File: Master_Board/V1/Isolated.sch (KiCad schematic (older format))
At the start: 0 parts

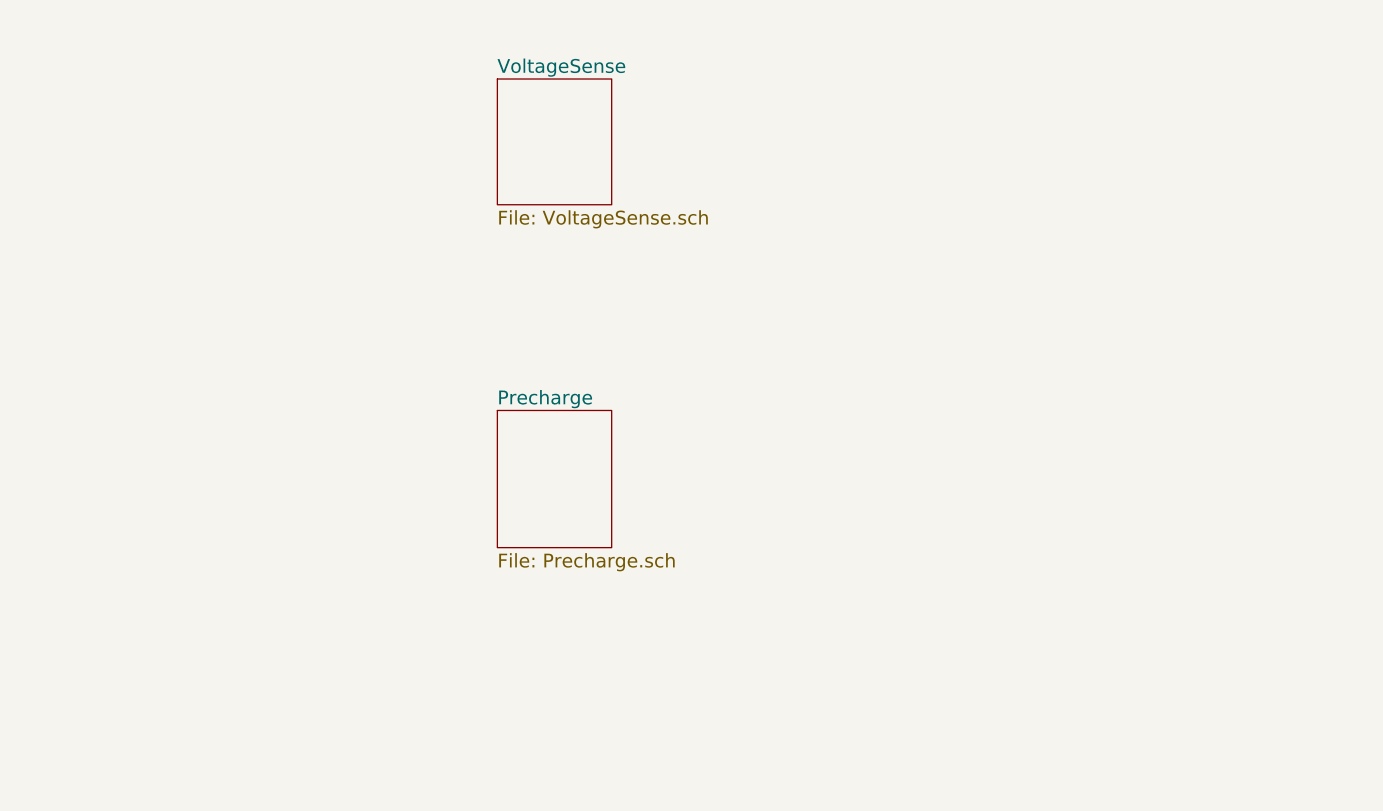
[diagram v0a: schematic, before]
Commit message: Add Master_Board modules
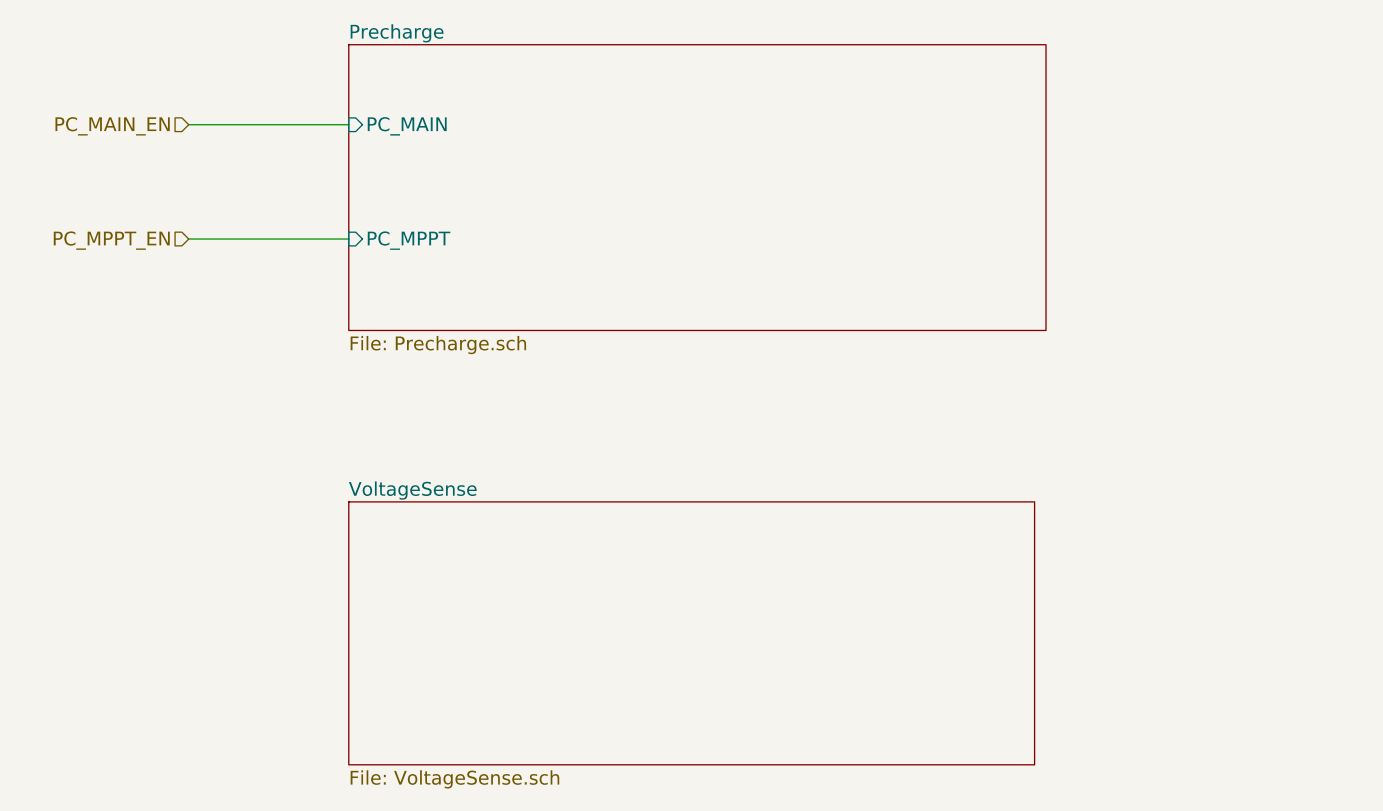
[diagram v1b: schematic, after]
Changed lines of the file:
@@
 $EndDescr
 $Sheet
-S 4700 2600 500  550
+S 4050 2450 3050 1250
+U 5941231F
+F0 "Precharge" 60
+F1 "Precharge.sch" 60
+F2 "PC_MAIN" I L 4050 2800 60
+F3 "PC_MPPT" I L 4050 3300 60
+$EndSheet
+Text HLabel 3350 2800 0    60   Input ~ 0
+PC_MAIN_EN
+$Sheet
+S 4050 4450 3000 1150
 U 5941231C
 F0 "VoltageSense" 60
 F1 "VoltageSense.sch" 60
 $EndSheet
-$Sheet
-S 4700 4050 500  600
-U 5941231F
-F0 "Precharge" 60
-F1 "Precharge.sch" 60
-$EndSheet
+Text HLabel 3350 3300 0    60   Input ~ 0
+PC_MPPT_EN
+Wire Wire Line
+	3350 2800 4050 2800
+Wire Wire Line
+	3350 3300 4050 3300
 $EndSCHEMATC

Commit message: git modify Master_board
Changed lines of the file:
@@
 F0 "VoltageSense" 60
 F1 "VoltageSense.sch" 60
+F2 "BP_VSense" I L 4050 4700 60
+F3 "VSense_EN" I L 4050 5000 60
+F4 "MPPT_VSense" I L 4050 5300 60
 $EndSheet
 Text HLabel 3350 3300 0    60   Input ~ 0
@@
 Wire Wire Line
 	3350 3300 4050 3300
+Wire Wire Line
+	4050 4700 3350 4700
+Wire Wire Line
+	4050 5000 3350 5000
+Wire Wire Line
+	4050 5300 3350 5300
+Text HLabel 3350 4700 0    60   Input ~ 0
+BP_VSense
+Text HLabel 3350 5000 0    60   Input ~ 0
+VSense_EN
+Text HLabel 3350 5300 0    60   Input ~ 0
+MPPT_VSense
 $EndSCHEMATC

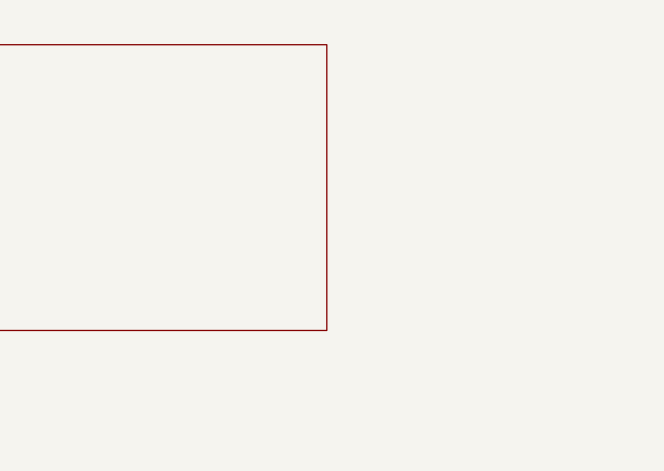
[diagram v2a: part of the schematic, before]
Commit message: Add page LedDriver
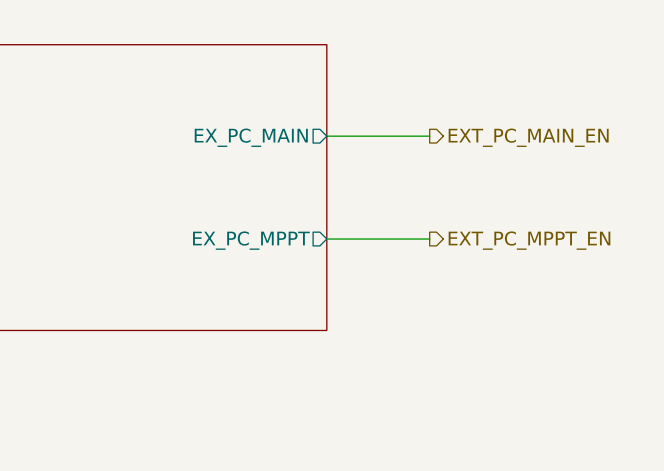
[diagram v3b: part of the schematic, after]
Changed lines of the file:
@@
 $Descr A4 11693 8268
 encoding utf-8
-Sheet 6 10
+Sheet 6 11
 Title ""
 Date ""
@@
 F2 "PC_MAIN" I L 4050 2800 60
 F3 "PC_MPPT" I L 4050 3300 60
+F4 "EX_PC_MAIN" O R 7100 2850 60
+F5 "EX_PC_MPPT" O R 7100 3300 60
 $EndSheet
 Text HLabel 3350 2800 0    60   Input ~ 0
@@
 Text HLabel 3350 5300 0    60   Input ~ 0
 MPPT_VSense
+Wire Wire Line
+	7100 2850 7550 2850
+Wire Wire Line
+	7100 3300 7550 3300
+Text HLabel 7550 2850 2    60   Output ~ 0
+EXT_PC_MAIN_EN
+Text HLabel 7550 3300 2    60   Output ~ 0
+EXT_PC_MPPT_EN
 $EndSCHEMATC
